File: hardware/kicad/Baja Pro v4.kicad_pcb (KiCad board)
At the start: 2 copper layers, 73 x 65 mm, 29 parts, among them J1 Thermistor, P1 Remote, P2 Power, P4 Flash, U1 FM24CL04B-GTR_C365762, U2 DC-DC stepdown, U3 AMS1117-3.3, U4 ESP32-WROOM-32

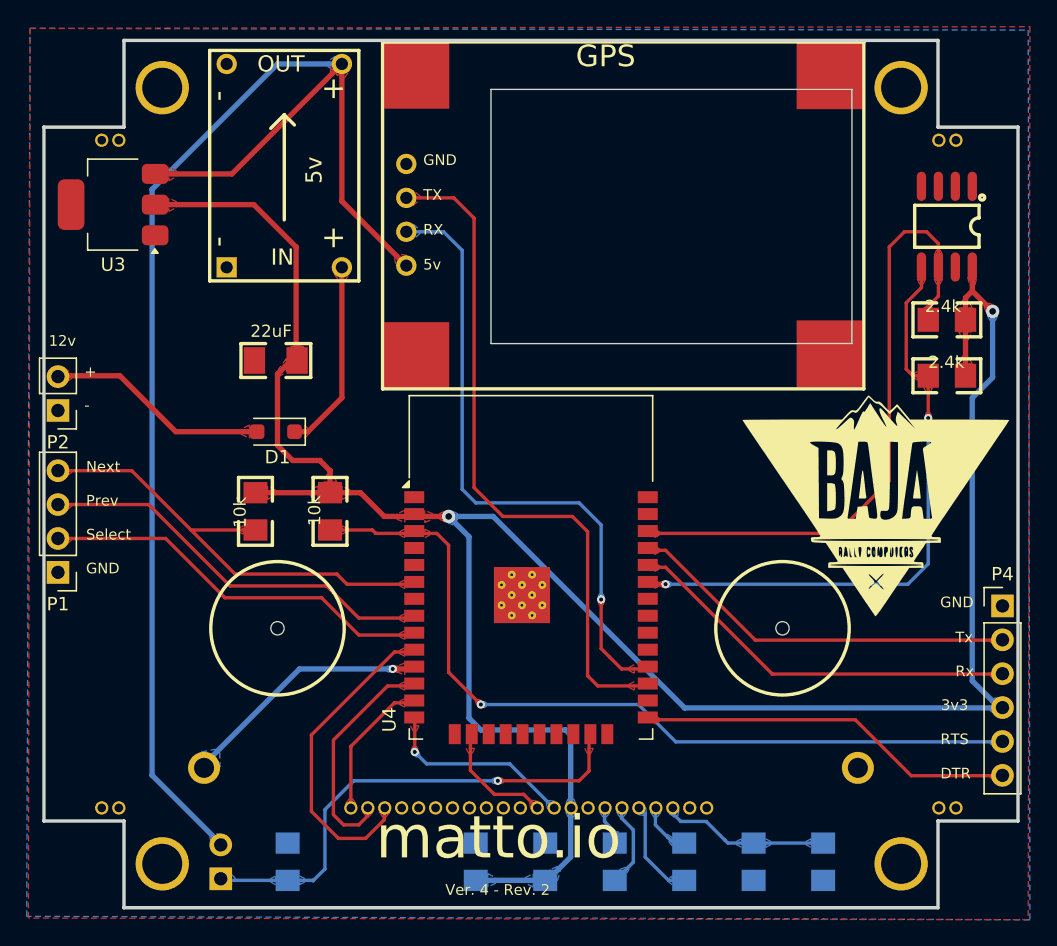
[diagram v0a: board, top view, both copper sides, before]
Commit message: Implement on board DCDC converter Run on 3.3V Replace thermistor with SMD one Change cable connectors to JST Rearrange tracks to help WiFi antenna clearance
Signed-off-by: Ilias Daradimos <judgedrid@gmail.com>
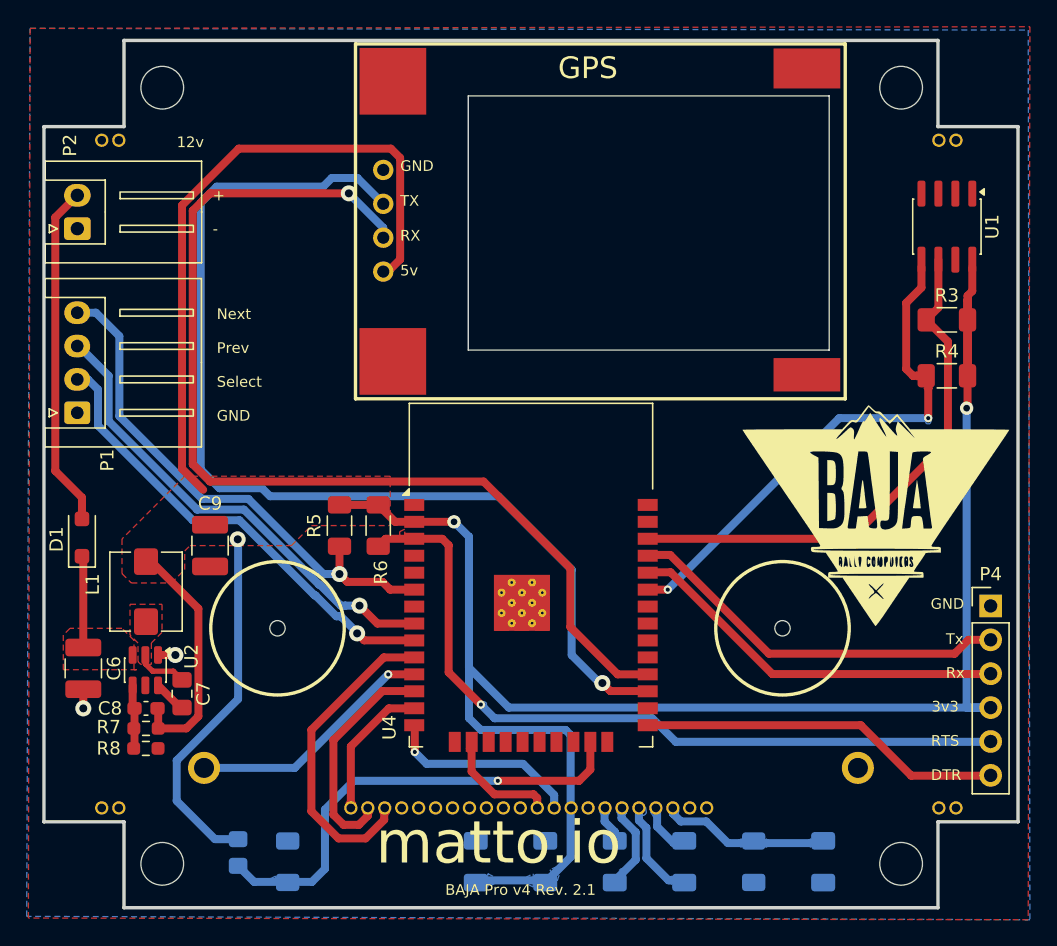
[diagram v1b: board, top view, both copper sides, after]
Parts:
- removed Hole_gge526: Hole_gge526, Baja Pro v4:Hole_gge526
- removed Hole_gge527: Hole_gge527, Baja Pro v4:Hole_gge527
- removed Pad_gge522: Pad_gge522, Baja Pro v4:Pad_gge522
- removed Pad_gge523: Pad_gge523, Baja Pro v4:Pad_gge523
- removed Pad_gge524: Pad_gge524, Baja Pro v4:Pad_gge524
- removed Pad_gge525: Pad_gge525, Baja Pro v4:Pad_gge525
- removed U3: AMS1117-3.3, Package_TO_SOT_SMD:SOT-223-3_TabPin2
- added C7: 100nF, Capacitor_SMD:C_0805_2012Metric_Pad1.18x1.45mm_HandSolder, F.Cu at (120.5, 119.1)
- added C8: 47pF, Capacitor_SMD:C_0603_1608Metric_Pad1.08x0.95mm_HandSolder, F.Cu at (117.8, 120.2)
- added C9: 47uF, Capacitor_SMD:C_1210_3225Metric_Pad1.33x2.70mm_HandSolder, F.Cu at (122.6, 108.0)
- added L1: 10uH, Inductor_SMD:L_Bourns_SRP5030T, F.Cu at (117.8, 111.5)
- added R7: 100k, Resistor_SMD:R_0603_1608Metric_Pad0.98x0.95mm_HandSolder, F.Cu at (117.8, 121.7)
- added R8: 22k, Resistor_SMD:R_0603_1608Metric_Pad0.98x0.95mm_HandSolder, F.Cu at (117.8, 123.2)
- added REF**: MountingHole_3.2mm_M3, MountingHole:MountingHole_3.2mm_M3, F.Cu at (174.4, 73.7)
- added REF**: ToolingHole_1.152mm, MountingHole:ToolingHole_1.152mm, F.Cu at (165.5, 114.2)
- added REF**: MountingHole_3.2mm_M3, MountingHole:MountingHole_3.2mm_M3, F.Cu at (119.0, 73.7)
- added REF**: ToolingHole_1.152mm, MountingHole:ToolingHole_1.152mm, F.Cu at (127.7, 114.2)
- added REF**: MountingHole_3.2mm_M3, MountingHole:MountingHole_3.2mm_M3, F.Cu at (119.0, 131.8)
- added REF**: MountingHole_3.2mm_M3, MountingHole:MountingHole_3.2mm_M3, F.Cu at (174.4, 131.8)
- C1, C2, C3, C4, C5: footprint Baja Pro v4:1206 -> Capacitor_SMD:C_1206_3216Metric_Pad1.33x1.80mm_HandSolder
- C6: value 22uF -> 10uF; footprint Baja Pro v4:1206 -> Capacitor_SMD:C_1210_3225Metric_Pad1.33x2.70mm_HandSolder
- J1: value Thermistor -> NTC 10K±1% 3950; footprint Connector_PinHeader_2.54mm:PinHeader_1x02_P2.54mm_Vertical -> Resistor_SMD:R_0805_2012Metric_Pad1.20x1.40mm_HandSolder
- P1: footprint Connector_PinHeader_2.54mm:PinHeader_1x04_P2.54mm_Vertical -> Connector_JST:JST_XH_S4B-XH-A_1x04_P2.50mm_Horizontal
- P2: footprint Connector_PinHeader_2.54mm:PinHeader_1x02_P2.54mm_Vertical -> Connector_JST:JST_XH_S2B-XH-A_1x02_P2.50mm_Horizontal
- R1, R2, R3, R4, R5, R6: footprint Baja Pro v4:1206 -> Resistor_SMD:R_1206_3216Metric_Pad1.30x1.75mm_HandSolder
- U1: footprint Baja Pro v4:SOIC-8_150MIL -> Package_SO:SOIC-8_3.9x4.9mm_P1.27mm
- U2: value DC-DC stepdown -> TPS54302; footprint Baja Pro v4:DC-DC STEPDOWN -> Package_TO_SOT_SMD:SOT-23-6
- moved U2 39.2 mm to (117.8, 117.3), turned to -90 degrees
- moved C6 27.2 mm to (113.1, 117.2), turned to -90 degrees
- moved D1 16.6 mm to (113.0, 107.4), turned to 90 degrees
- moved P2 13.7 mm to (112.7, 84.2), turned to 90 degrees
- moved P1 12.0 mm to (112.6, 98.0), turned to 90 degrees
- moved R6 6.39 mm to (132.3, 106.5)
- moved R5 3.76 mm to (135.2, 106.5)
- moved J1 2.36 mm to (124.7, 131.0), turned to 90 degrees
- moved GPS1 1.78 mm to (133.8, 70.7)
- moved P4 0.89 mm to (181.1, 112.5)
- moved U4 0.58 mm to (146.7, 113.2)
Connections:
- C6 pad 1: GND -> /VIN
- C6 pad 2: 3V3 -> GND
- D1 pad 1: Net-(D1-K) -> /VIN
- GPS1 pad 4: 5V -> 3V3
- J1 pad 2: 5V -> 3V3
- U2 pad 2: Net-(D1-K) -> Net-(U2-SW)
- U2 pad 3: 5V -> /VIN
- U2 pad 4: GND -> Net-(U2-FB)
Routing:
- net 5V: track 103.9 -> 0.00 mm
- net 3V3: track 179.1 -> 234.4 mm, vias 2 -> 3
- net GPS_RX: track 47.3 -> 78.8 mm
- net GPS_TX: track 51.1 -> 79.4 mm, vias 0 -> 1
- net Net-(D1-K): track 14.1 -> 0.00 mm
- net Net-(D1-A): track 16.2 -> 25.8 mm
- net MEM_SCL: track 48.1 -> 40.2 mm
- net /VIN: track 0.00 -> 6.74 mm
- net MEM_SDA: track 46.0 -> 39.5 mm
- net R_PREV: track 29.9 -> 35.7 mm, vias 0 -> 1
- net R_SELECT: track 29.4 -> 35.0 mm, vias 0 -> 1
- net R_NEXT: track 34.8 -> 39.4 mm, vias 0 -> 1
- net Net-(U2-FB): track 0.00 -> 4.53 mm
- net FLASH_RTS: track 62.3 -> 58.0 mm
- net Net-(U2-SW): track 0.00 -> 3.91 mm
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- added copper zone on F.Cu, net /VIN
- added copper zone on F.Cu, net Net-(U2-SW)
- removed copper zone on B.Cu, net 5V
- removed copper zone on F.Cu, net 5V
- removed copper zone on B.Cu, net DISPLAY_BL
- removed copper zone on F.Cu, net DISPLAY_BL
- removed copper zone on B.Cu, net GPS_RX
- removed copper zone on F.Cu, net GPS_RX
- removed copper zone on F.Cu, net GPS_TX
- removed copper zone on F.Cu, net MEM_SCL
- removed copper zone on F.Cu, net Net-(D1-A)
- removed copper zone on F.Cu, net Net-(D1-K)
- removed copper zone on F.Cu, net R_NEXT
- removed copper zone on F.Cu, net R_PREV
- removed copper zone on F.Cu, net R_SELECT
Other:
- outline, holes or cut-outs redrawn
- board text added: "${TITLE} Rev. ${REVISION}"
- board text added: "KEEP-OUT ZONE"
- board text removed: "Ver. 4 - Rev. 2"

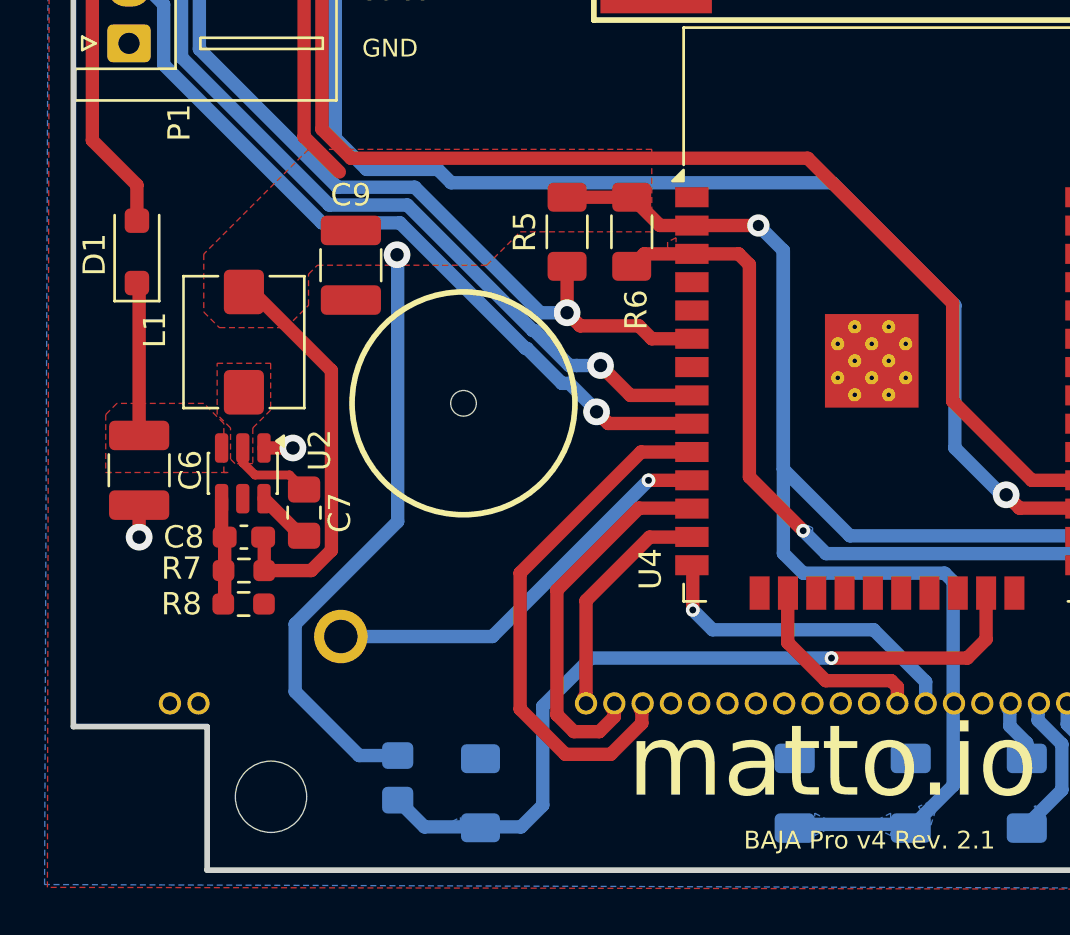
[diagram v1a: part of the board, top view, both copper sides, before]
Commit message: Add part numbers Generate BOM Generate HTML assembly
Signed-off-by: Ilias Daradimos <judgedrid@gmail.com>
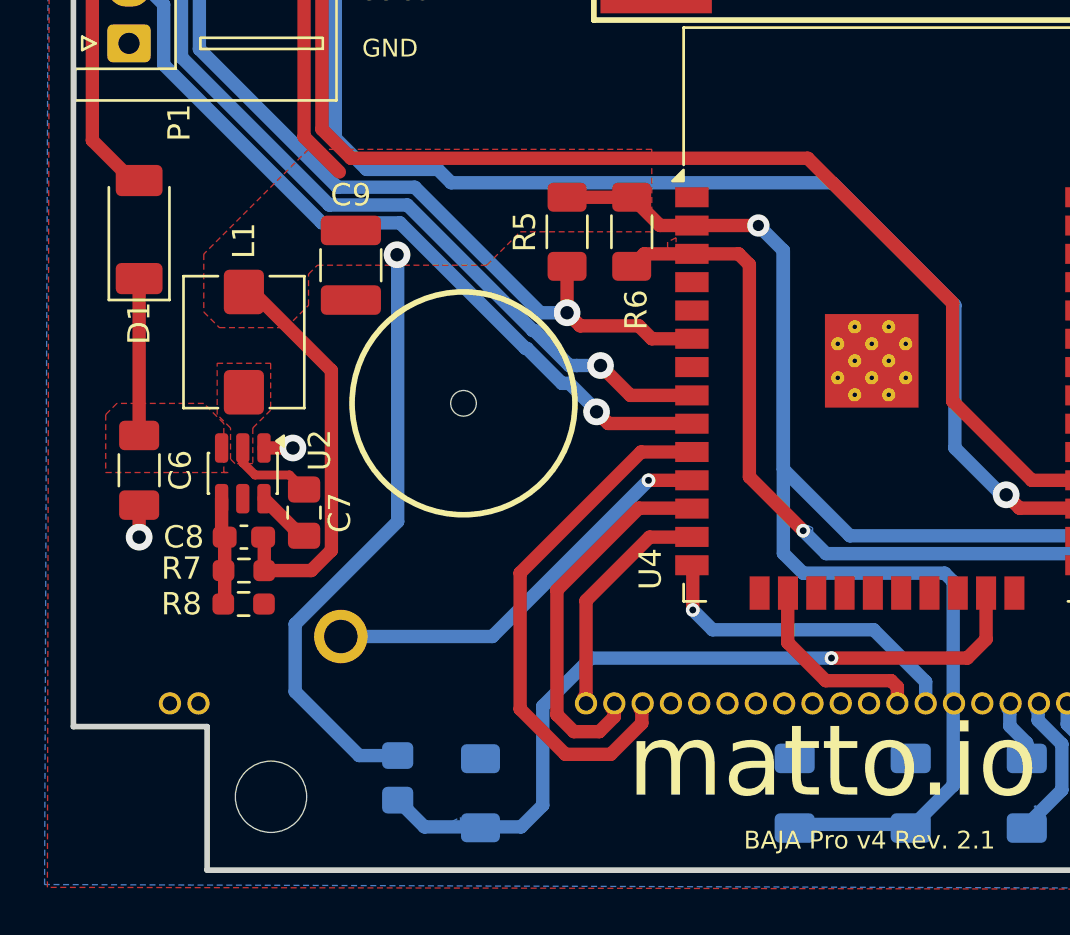
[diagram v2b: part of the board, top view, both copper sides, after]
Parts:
- C6: footprint Capacitor_SMD:C_1210_3225Metric_Pad1.33x2.70mm_HandSolder -> Capacitor_SMD:C_1206_3216Metric_Pad1.33x1.80mm_HandSolder
- D1: value 1N4007 -> PU3BFSH; footprint Diode_SMD:D_SOD-123F -> Diode_SMD:D_SOD-128
- moved D1 1.00 mm to (113.1, 106.4)
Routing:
- net Net-(D1-A): track 25.8 -> 24.2 mm
- removed copper zone on B.Cu, net 3V3
